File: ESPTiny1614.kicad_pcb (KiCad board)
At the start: 2 copper layers, 33 x 23.9 mm, 23 parts, among them J1 Conn_01x10_Male, J2 Conn_01x10_Male, J3 Conn_01x04_Male, U1 ESP-01v090, U2 ATtiny1614-SS, U3 MCP1700-3302E_TO92, Y1 Crystal 32.768kHz

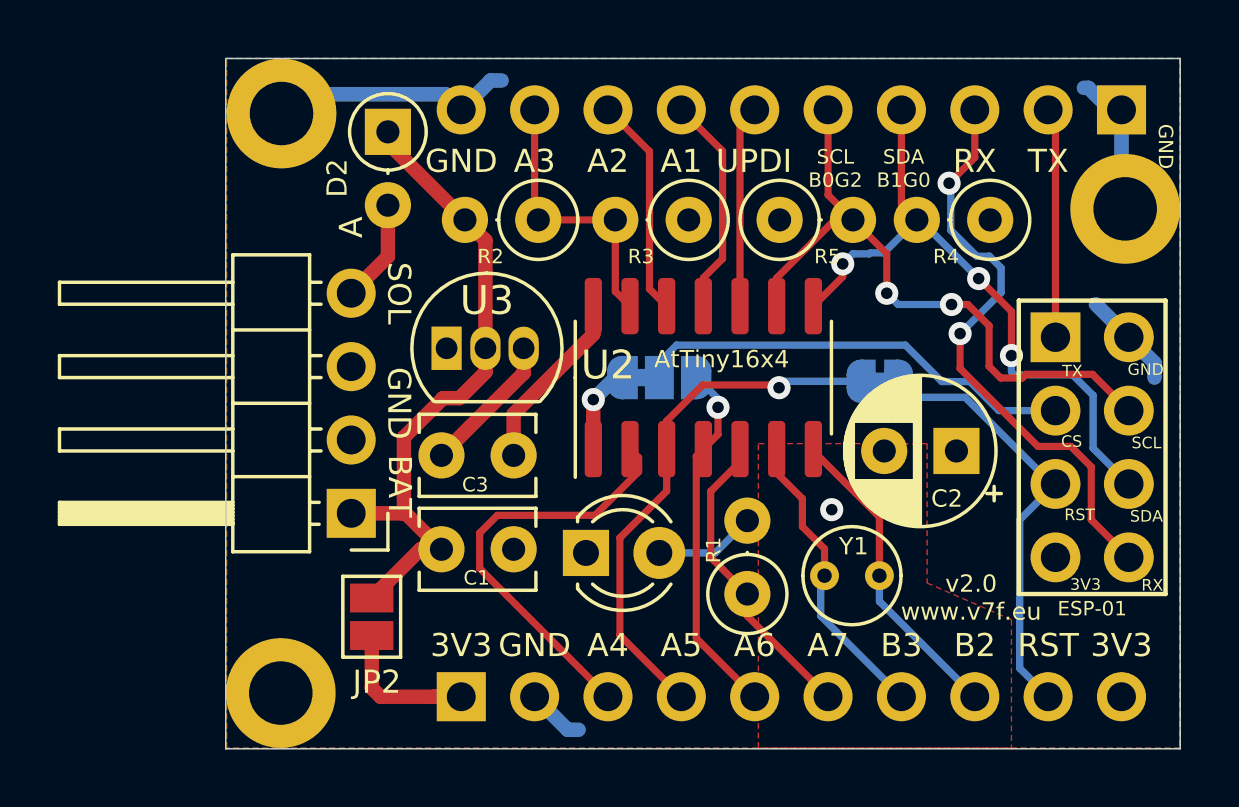
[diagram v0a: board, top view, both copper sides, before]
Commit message: Update layout of MCP1700 and power pins
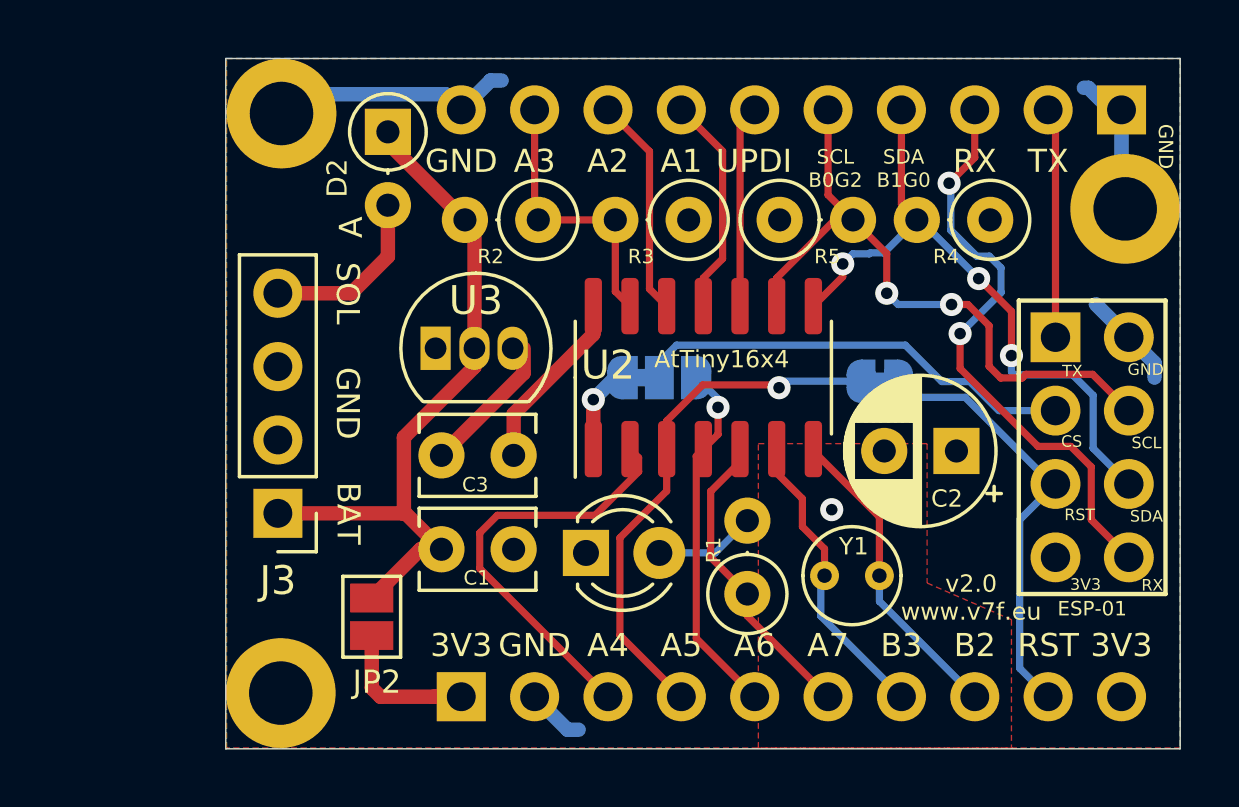
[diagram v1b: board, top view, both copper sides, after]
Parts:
- J3: footprint Connector_PinHeader_2.54mm:PinHeader_1x04_P2.54mm_Horizontal -> Connector_PinHeader_2.54mm:PinHeader_1x04_P2.54mm_Vertical
- moved J3 2.54 mm to (40.9, 56.1)
- moved U3 0.38 mm to (46.5, 50.4)
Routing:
- net Net-(D2-Pad2): track 3.57 -> 6.11 mm
- net +BATT: track 22.9 -> 24.7 mm

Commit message: Add capacitors to 32768 crystal
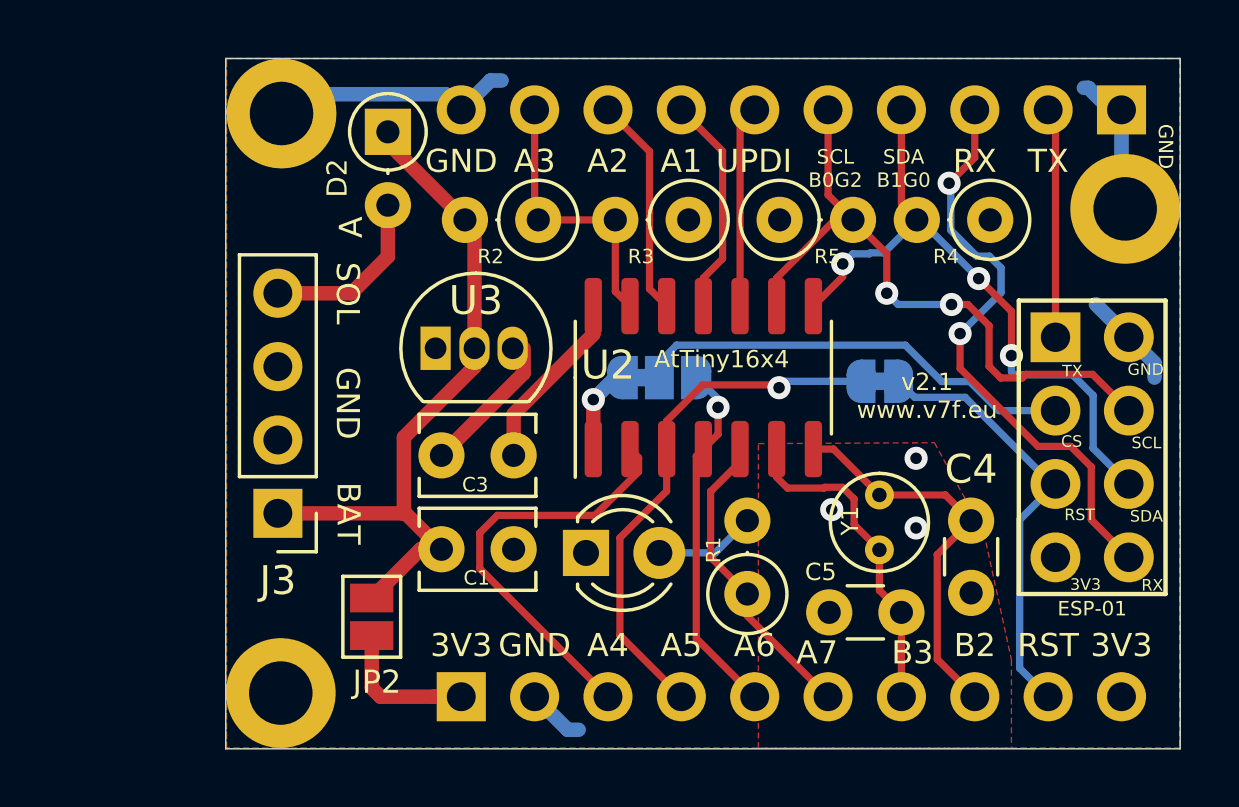
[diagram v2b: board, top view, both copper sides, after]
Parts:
- removed C2: 100u, Capacitor_THT:CP_Radial_D5.0mm_P2.50mm
- added C4: 10p, Capacitor_THT:C_Disc_D3.0mm_W1.6mm_P2.50mm, F.Cu at (64.9, 56.4)
- added C5: 10p, Capacitor_THT:C_Disc_D3.0mm_W1.6mm_P2.50mm, F.Cu at (62.5, 59.6)
- moved Y1 2.79 mm to (61.7, 55.5), turned to 270 degrees
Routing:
- net /B2: track 10.9 -> 13.6 mm
- net /B3: track 10.5 -> 11.5 mm
- net GND: vias 1 -> 3
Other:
- board text added: "v2.1 www.v7f.eu"
- board text removed: "v2.0 www.v7f.eu"

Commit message: Better silk 1614 and improve battery code
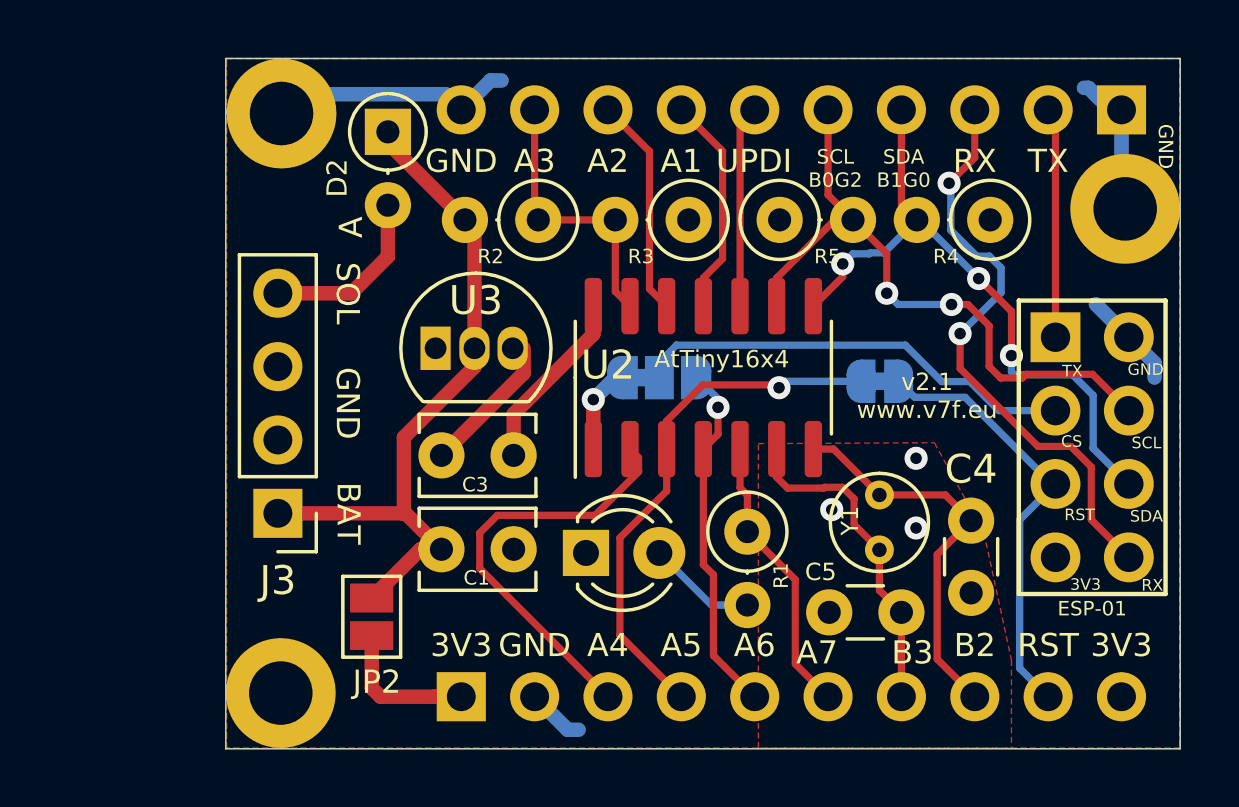
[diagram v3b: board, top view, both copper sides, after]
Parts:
- moved R1 2.16 mm to (57.1, 56.8), turned to 270 degrees
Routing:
- net Net-(D1-Pad2): track 3.74 -> 4.56 mm
